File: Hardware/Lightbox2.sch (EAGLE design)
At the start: 12 parts, among them IC1 7805T, U1 328P

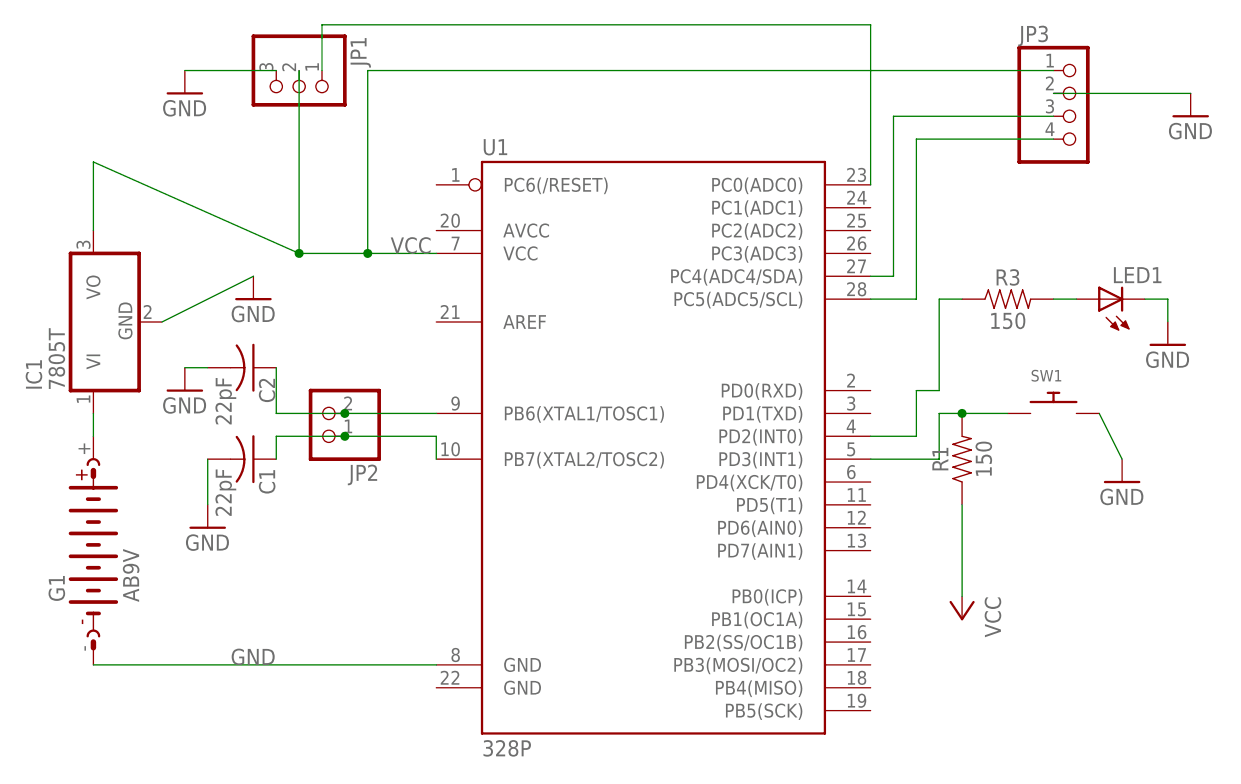
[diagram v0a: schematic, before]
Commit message: Increase trace thickness and replace wrong components
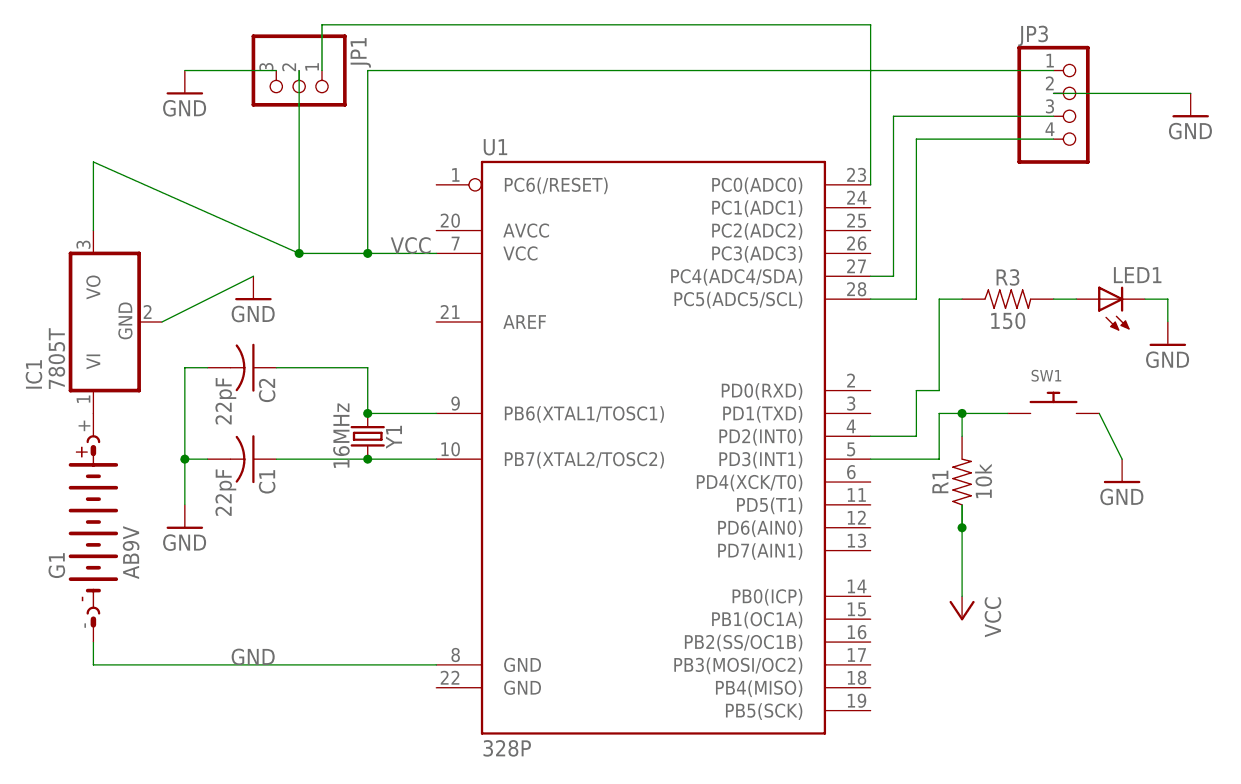
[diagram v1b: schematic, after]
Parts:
- removed JP2: (no value), pinhead:PINHD-1X2
- added Y1: 16MHz, SparkFun-Clocks:CRYSTAL-16MHZPTH-HC49US
- R1: value 150 -> 10k; device SparkFun-Resistors:150OHM-0603-1/10W-1% -> SparkFun-Resistors:10KOHM-0603-1/10W-1%
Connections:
- net XTAL1: now also Y1.1; no longer JP2.2
- net XTAL2: now also Y1.2; no longer JP2.1
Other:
- moved on the sheet: G1, R1
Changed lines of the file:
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@@
 <part name="JP3" library="pinhead" library_urn="urn:adsk.eagle:library:325" deviceset="PINHD-1X4" device="" package3d_urn="urn:adsk.eagle:package:22407/2"/>
 <part name="G1" library="battery" library_urn="urn:adsk.eagle:library:109" deviceset="AB9V" device="" package3d_urn="urn:adsk.eagle:package:4600/1"/>
-<part name="R1" library="SparkFun-Resistors" library_urn="urn:adsk.eagle:library:532" deviceset="150OHM" device="-0603-1/10W-1%" package3d_urn="urn:adsk.eagle:package:39650/1" value="150"/>
-<part name="JP2" library="pinhead" library_urn="urn:adsk.eagle:library:325" deviceset="PINHD-1X2" device="" package3d_urn="urn:adsk.eagle:package:22435/2"/>
 <part name="C1" library="adafruit" library_urn="urn:adsk.eagle:library:420" deviceset="C-US" device="025-024X044" package3d_urn="urn:adsk.eagle:package:6240324/1" value="22pF"/>
 <part name="C2" library="adafruit" library_urn="urn:adsk.eagle:library:420" deviceset="C-US" device="025-024X044" package3d_urn="urn:adsk.eagle:package:6240324/1" value="22pF"/>
@@
 <part name="GND2" library="supply1" library_urn="urn:adsk.eagle:library:371" deviceset="GND" device=""/>
 <part name="GND3" library="supply1" library_urn="urn:adsk.eagle:library:371" deviceset="GND" device=""/>
-<part name="GND4" library="supply1" library_urn="urn:adsk.eagle:library:371" deviceset="GND" device=""/>
 <part name="IC1" library="adafruit" library_urn="urn:adsk.eagle:library:420" deviceset="78*" device="T" package3d_urn="urn:adsk.eagle:package:6240670/1" technology="05"/>
 <part name="R3" library="SparkFun-Resistors" library_urn="urn:adsk.eagle:library:532" deviceset="150OHM" device="-0603-1/10W-1%" package3d_urn="urn:adsk.eagle:package:39650/1" value="150"/>
@@
 <part name="GND7" library="supply1" library_urn="urn:adsk.eagle:library:371" deviceset="GND" device=""/>
 <part name="P+1" library="supply1" library_urn="urn:adsk.eagle:library:371" deviceset="VCC" device=""/>
+<part name="Y1" library="SparkFun-Clocks" library_urn="urn:adsk.eagle:library:511" deviceset="CRYSTAL-16MHZ" device="PTH-HC49US" package3d_urn="urn:adsk.eagle:package:37515/1" value="16MHz"/>
+<part name="R1" library="SparkFun-Resistors" library_urn="urn:adsk.eagle:library:532" deviceset="10KOHM" device="-0603-1/10W-1%" package3d_urn="urn:adsk.eagle:package:39650/1" value="10k"/>
 </parts>
 <sheets>
@@
 <attribute name="VALUE" x="95.25" y="78.74" size="1.778" layer="96"/>
 </instance>
-<instance part="G1" gate="G$1" x="-7.62" y="38.1" rot="R90">
-<attribute name="NAME" x="-10.795" y="32.385" size="1.778" layer="95" rot="R90"/>
-<attribute name="VALUE" x="-2.54" y="32.385" size="1.778" layer="96" rot="R90"/>
-</instance>
-<instance part="R1" gate="G$1" x="88.9" y="48.26" rot="R90">
-<attribute name="NAME" x="87.376" y="48.26" size="1.778" layer="95" font="vector" rot="R90" align="bottom-center"/>
-<attribute name="VALUE" x="90.424" y="48.26" size="1.778" layer="96" font="vector" rot="R90" align="top-center"/>
-</instance>
-<instance part="JP2" gate="G$1" x="17.78" y="53.34" rot="R180">
-<attribute name="NAME" x="24.13" y="47.625" size="1.778" layer="95" rot="R180"/>
-<attribute name="VALUE" x="24.13" y="58.42" size="1.778" layer="96" rot="R180"/>
+<instance part="G1" gate="G$1" x="-7.62" y="40.64" rot="R90">
+<attribute name="NAME" x="-10.795" y="34.925" size="1.778" layer="95" rot="R90"/>
+<attribute name="VALUE" x="-2.54" y="34.925" size="1.778" layer="96" rot="R90"/>
 </instance>
 <instance part="C1" gate="G$1" x="10.16" y="48.26" rot="R270">
@@
 <attribute name="VALUE" x="109.22" y="58.42" size="1.778" layer="96"/>
 </instance>
-<instance part="GND3" gate="1" x="5.08" y="40.64">
-<attribute name="VALUE" x="2.54" y="38.1" size="1.778" layer="96"/>
-</instance>
-<instance part="GND4" gate="1" x="2.54" y="55.88">
-<attribute name="VALUE" x="0" y="53.34" size="1.778" layer="96"/>
+<instance part="GND3" gate="1" x="2.54" y="40.64">
+<attribute name="VALUE" x="0" y="38.1" size="1.778" layer="96"/>
 </instance>
 <instance part="IC1" gate="A1" x="-7.62" y="63.5" rot="R90">
@@
 <instance part="P+1" gate="VCC" x="88.9" y="30.48" rot="R180">
 <attribute name="VALUE" x="91.44" y="33.02" size="1.778" layer="96" rot="R270"/>
+</instance>
+<instance part="Y1" gate="G$1" x="22.86" y="50.8" rot="R270">
+<attribute name="NAME" x="24.892" y="50.8" size="1.778" layer="95" font="vector" rot="R270" align="bottom-center"/>
+<attribute name="VALUE" x="20.828" y="50.8" size="1.778" layer="96" font="vector" rot="R270" align="top-center"/>
+</instance>
+<instance part="R1" gate="G$1" x="88.9" y="45.72" rot="R90">
+<attribute name="NAME" x="87.376" y="45.72" size="1.778" layer="95" font="vector" rot="R90" align="bottom-center"/>
+<attribute name="VALUE" x="90.424" y="45.72" size="1.778" layer="96" font="vector" rot="R90" align="top-center"/>
 </instance>
 </instances>
@@
 </segment>
 </net>
-<net name="XTAL1" class="0">
-<segment>
-<pinref part="JP2" gate="G$1" pin="2"/>
-<pinref part="U1" gate="G$1" pin="PB6(XTAL1/TOSC1)"/>
-<wire x1="20.32" y1="53.34" x2="30.48" y2="53.34" width="0.1524" layer="91"/>
-<wire x1="20.32" y1="53.34" x2="12.7" y2="53.34" width="0.1524" layer="91"/>
-<junction x="20.32" y="53.34"/>
-<pinref part="C2" gate="G$1" pin="1"/>
-<wire x1="12.7" y1="53.34" x2="12.7" y2="58.42" width="0.1524" layer="91"/>
-</segment>
-</net>
-<net name="XTAL2" class="0">
-<segment>
-<pinref part="JP2" gate="G$1" pin="1"/>
-<wire x1="20.32" y1="50.8" x2="30.48" y2="50.8" width="0.1524" layer="91"/>
-<pinref part="U1" gate="G$1" pin="PB7(XTAL2/TOSC2)"/>
-<wire x1="30.48" y1="50.8" x2="30.48" y2="48.26" width="0.1524" layer="91"/>
-<pinref part="C1" gate="G$1" pin="1"/>
-<wire x1="12.7" y1="48.26" x2="12.7" y2="50.8" width="0.1524" layer="91"/>
-<wire x1="12.7" y1="50.8" x2="20.32" y2="50.8" width="0.1524" layer="91"/>
-<junction x="20.32" y="50.8"/>
-</segment>
-</net>
 <net name="GND" class="0">
-<segment>
-<pinref part="GND4" gate="1" pin="GND"/>
-<pinref part="C2" gate="G$1" pin="2"/>
-<wire x1="2.54" y1="58.42" x2="5.08" y2="58.42" width="0.1524" layer="91"/>
-</segment>
-<segment>
-<pinref part="C1" gate="G$1" pin="2"/>
-<pinref part="GND3" gate="1" pin="GND"/>
-<wire x1="5.08" y1="48.26" x2="5.08" y2="43.18" width="0.1524" layer="91"/>
-</segment>
 <segment>
 <pinref part="LED1" gate="G$1" pin="C"/>
@@
 <pinref part="G1" gate="G$1" pin="-"/>
 <pinref part="U1" gate="G$1" pin="GND@1"/>
+<label x="7.62" y="25.4" size="1.778" layer="95"/>
+<wire x1="-7.62" y1="27.94" x2="-7.62" y2="25.4" width="0.1524" layer="91"/>
 <wire x1="-7.62" y1="25.4" x2="30.48" y2="25.4" width="0.1524" layer="91"/>
-<label x="7.62" y="25.4" size="1.778" layer="95"/>
+</segment>
+<segment>
+<pinref part="C1" gate="G$1" pin="2"/>
+<wire x1="5.08" y1="48.26" x2="2.54" y2="48.26" width="0.1524" layer="91"/>
+<pinref part="GND3" gate="1" pin="GND"/>
+<wire x1="2.54" y1="48.26" x2="2.54" y2="43.18" width="0.1524" layer="91"/>
+<pinref part="C2" gate="G$1" pin="2"/>
+<wire x1="2.54" y1="58.42" x2="5.08" y2="58.42" width="0.1524" layer="91"/>
+<wire x1="2.54" y1="58.42" x2="2.54" y2="48.26" width="0.1524" layer="91"/>
+<junction x="2.54" y="48.26"/>
 </segment>
 </net>
@@
 <pinref part="G1" gate="G$1" pin="+"/>
 <pinref part="IC1" gate="A1" pin="VI"/>
-<wire x1="-7.62" y1="50.8" x2="-7.62" y2="53.34" width="0.1524" layer="91"/>
 </segment>
 </net>
 <net name="VCC" class="0">
 <segment>
+<pinref part="P+1" gate="VCC" pin="VCC"/>
+<wire x1="88.9" y1="33.02" x2="88.9" y2="40.64" width="0.1524" layer="91"/>
 <pinref part="R1" gate="G$1" pin="1"/>
-<pinref part="P+1" gate="VCC" pin="VCC"/>
-<wire x1="88.9" y1="33.02" x2="88.9" y2="43.18" width="0.1524" layer="91"/>
+<wire x1="88.9" y1="40.64" x2="88.9" y2="43.18" width="0.1524" layer="91"/>
+<junction x="88.9" y="40.64"/>
 </segment>
 <segment>
@@
 <net name="PD3" class="0">
 <segment>
-<pinref part="R1" gate="G$1" pin="2"/>
 <pinref part="SW1" gate="G$1" pin="P$1"/>
 <wire x1="93.98" y1="53.34" x2="88.9" y2="53.34" width="0.1524" layer="91"/>
 <pinref part="U1" gate="G$1" pin="PD3(INT1)"/>
+<wire x1="88.9" y1="53.34" x2="86.36" y2="53.34" width="0.1524" layer="91"/>
 <wire x1="78.74" y1="48.26" x2="86.36" y2="48.26" width="0.1524" layer="91"/>
 <wire x1="86.36" y1="48.26" x2="86.36" y2="53.34" width="0.1524" layer="91"/>
-<wire x1="86.36" y1="53.34" x2="88.9" y2="53.34" width="0.1524" layer="91"/>
+<pinref part="R1" gate="G$1" pin="2"/>
+<wire x1="88.9" y1="50.8" x2="88.9" y2="53.34" width="0.1524" layer="91"/>
 <junction x="88.9" y="53.34"/>
 </segment>
@@
 </segment>
 </net>
+<net name="XTAL1" class="0">
+<segment>
+<pinref part="Y1" gate="G$1" pin="1"/>
+<pinref part="U1" gate="G$1" pin="PB6(XTAL1/TOSC1)"/>
+<wire x1="22.86" y1="53.34" x2="30.48" y2="53.34" width="0.1524" layer="91"/>
+<pinref part="C2" gate="G$1" pin="1"/>
+<wire x1="22.86" y1="53.34" x2="22.86" y2="58.42" width="0.1524" layer="91"/>
+<wire x1="22.86" y1="58.42" x2="12.7" y2="58.42" width="0.1524" layer="91"/>
+<junction x="22.86" y="53.34"/>
+</segment>
+</net>
+<net name="XTAL2" class="0">
+<segment>
+<pinref part="U1" gate="G$1" pin="PB7(XTAL2/TOSC2)"/>
+<pinref part="Y1" gate="G$1" pin="2"/>
+<wire x1="30.48" y1="48.26" x2="22.86" y2="48.26" width="0.1524" layer="91"/>
+<pinref part="C1" gate="G$1" pin="1"/>
+<wire x1="22.86" y1="48.26" x2="12.7" y2="48.26" width="0.1524" layer="91"/>
+<junction x="22.86" y="48.26"/>
+</segment>
+</net>

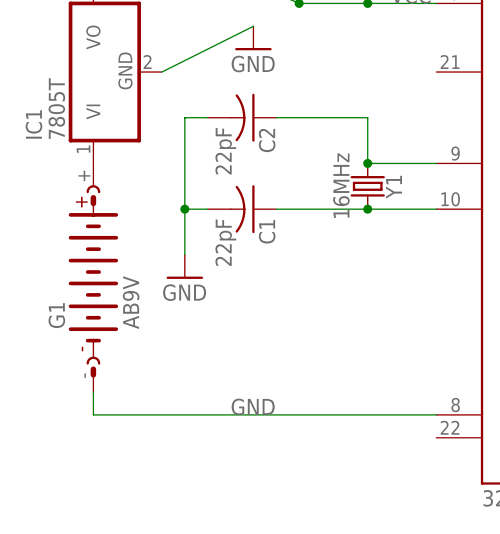
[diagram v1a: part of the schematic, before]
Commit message: Add dimensions and replace battery with 2pin header
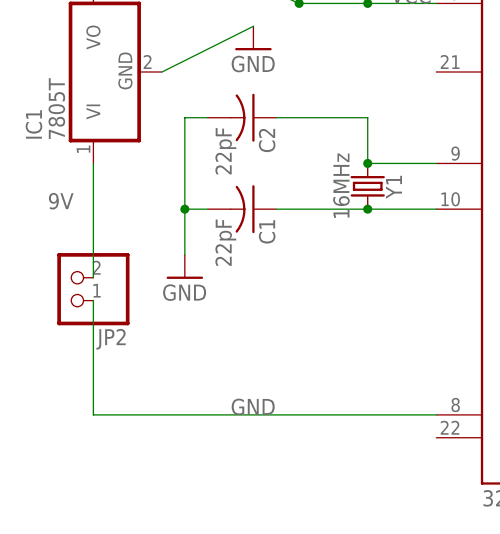
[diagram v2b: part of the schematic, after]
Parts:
- removed G1: AB9V, battery:AB9V
- added JP2: (no value), pinhead:PINHD-1X2
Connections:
- net 9V: now also JP2.2; no longer G1.+
- net GND: now also JP2.1; no longer G1.-
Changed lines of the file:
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@@
 <part name="JP1" library="adafruit" library_urn="urn:adsk.eagle:library:420" deviceset="PINHD-1X3" device="" package3d_urn="urn:adsk.eagle:package:6240710/1"/>
 <part name="JP3" library="pinhead" library_urn="urn:adsk.eagle:library:325" deviceset="PINHD-1X4" device="" package3d_urn="urn:adsk.eagle:package:22407/2"/>
-<part name="G1" library="battery" library_urn="urn:adsk.eagle:library:109" deviceset="AB9V" device="" package3d_urn="urn:adsk.eagle:package:4600/1"/>
 <part name="C1" library="adafruit" library_urn="urn:adsk.eagle:library:420" deviceset="C-US" device="025-024X044" package3d_urn="urn:adsk.eagle:package:6240324/1" value="22pF"/>
 <part name="C2" library="adafruit" library_urn="urn:adsk.eagle:library:420" deviceset="C-US" device="025-024X044" package3d_urn="urn:adsk.eagle:package:6240324/1" value="22pF"/>
@@
 <part name="Y1" library="SparkFun-Clocks" library_urn="urn:adsk.eagle:library:511" deviceset="CRYSTAL-16MHZ" device="PTH-HC49US" package3d_urn="urn:adsk.eagle:package:37515/1" value="16MHz"/>
 <part name="R1" library="SparkFun-Resistors" library_urn="urn:adsk.eagle:library:532" deviceset="10KOHM" device="-0603-1/10W-1%" package3d_urn="urn:adsk.eagle:package:39650/1" value="10k"/>
+<part name="JP2" library="pinhead" library_urn="urn:adsk.eagle:library:325" deviceset="PINHD-1X2" device="" package3d_urn="urn:adsk.eagle:package:22435/2"/>
 </parts>
 <sheets>
@@
 <attribute name="VALUE" x="95.25" y="78.74" size="1.778" layer="96"/>
 </instance>
-<instance part="G1" gate="G$1" x="-7.62" y="40.64" rot="R90">
-<attribute name="NAME" x="-10.795" y="34.925" size="1.778" layer="95" rot="R90"/>
-<attribute name="VALUE" x="-2.54" y="34.925" size="1.778" layer="96" rot="R90"/>
-</instance>
 <instance part="C1" gate="G$1" x="10.16" y="48.26" rot="R270">
 <attribute name="NAME" x="10.795" y="47.244" size="1.778" layer="95" rot="R270"/>
@@
 <attribute name="NAME" x="87.376" y="45.72" size="1.778" layer="95" font="vector" rot="R90" align="bottom-center"/>
 <attribute name="VALUE" x="90.424" y="45.72" size="1.778" layer="96" font="vector" rot="R90" align="top-center"/>
+</instance>
+<instance part="JP2" gate="G$1" x="-10.16" y="40.64" rot="R180">
+<attribute name="NAME" x="-3.81" y="34.925" size="1.778" layer="95" rot="R180"/>
+<attribute name="VALUE" x="-3.81" y="45.72" size="1.778" layer="96" rot="R180"/>
 </instance>
 </instances>
@@
 </segment>
 <segment>
-<pinref part="G1" gate="G$1" pin="-"/>
 <pinref part="U1" gate="G$1" pin="GND@1"/>
 <label x="7.62" y="25.4" size="1.778" layer="95"/>
-<wire x1="-7.62" y1="27.94" x2="-7.62" y2="25.4" width="0.1524" layer="91"/>
 <wire x1="-7.62" y1="25.4" x2="30.48" y2="25.4" width="0.1524" layer="91"/>
+<pinref part="JP2" gate="G$1" pin="1"/>
+<wire x1="-7.62" y1="25.4" x2="-7.62" y2="38.1" width="0.1524" layer="91"/>
 </segment>
 <segment>
@@
 <wire x1="2.54" y1="58.42" x2="2.54" y2="48.26" width="0.1524" layer="91"/>
 <junction x="2.54" y="48.26"/>
-</segment>
-</net>
-<net name="9V" class="0">
-<segment>
-<pinref part="G1" gate="G$1" pin="+"/>
-<pinref part="IC1" gate="A1" pin="VI"/>
 </segment>
 </net>
@@
 </segment>
 </net>
+<net name="9V" class="0">
+<segment>
+<pinref part="JP2" gate="G$1" pin="2"/>
+<pinref part="IC1" gate="A1" pin="VI"/>
+<wire x1="-7.62" y1="40.64" x2="-7.62" y2="53.34" width="0.1524" layer="91"/>
+<label x="-12.7" y="48.26" size="1.778" layer="95"/>
+</segment>
+</net>
